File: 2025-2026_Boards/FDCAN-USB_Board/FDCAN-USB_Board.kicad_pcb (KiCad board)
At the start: 2 copper layers, 54 parts, among them J1 USB4110GFA, J2 Conn_01x03_Socket, J3 Conn_01x03_Socket, J4 Conn_01x02_Pin, J5 Conn_01x02_Pin, J6 Conn_ARM_JTAG_SWD_10, U1 AMS1117-3.3, U2 USBLC6-2SC6, U3 STM32G474CETx, U4 TCAN1057AEV-Q1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

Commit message: microcontroller pin update
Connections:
- net USB_N renamed USB_DM
- net USB_P renamed USB_DP
- U3 pad 10: LED_Debug2 -> LED_RX_1
- U3 pad 12: unconnected-(U3-PA4-Pad12) -> LED_TX_1
- U3 pad 13: LED_RX_1 -> unconnected-(U3-PA5-Pad13)
- U3 pad 14: LED_TX_1 -> LED_RX_2
- U3 pad 17: LED_RX_2 -> unconnected-(U3-PB1-Pad17)
- U3 pad 2: unconnected-(U3-PC13-Pad2) -> LED_Debug1
- U3 pad 4: unconnected-(U3-PC15-Pad4) -> LED_Debug2
- U3 pad 9: LED_Debug1 -> unconnected-(U3-PA1-Pad9)
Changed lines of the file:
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@@
 	(net 37 "SWCLK")
 	(net 38 "SWDIO")
-	(net 39 "USB_N")
-	(net 40 "USB_P")
-	(net 41 "unconnected-(U3-PC15-Pad4)")
+	(net 39 "USB_DM")
+	(net 40 "USB_DP")
+	(net 41 "unconnected-(U3-PA1-Pad9)")
 	(net 42 "unconnected-(U3-PB15-Pad29)")
 	(net 43 "unconnected-(U3-PA7-Pad15)")
@@
 	(net 48 "unconnected-(U3-PF0-Pad5)")
 	(net 49 "unconnected-(U3-PA3-Pad11)")
-	(net 50 "unconnected-(U3-PC13-Pad2)")
+	(net 50 "unconnected-(U3-PB1-Pad17)")
 	(net 51 "unconnected-(U3-PB7-Pad44)")
 	(net 52 "unconnected-(U3-PA10-Pad32)")
@@
 	(net 62 "unconnected-(U3-PF1-Pad6)")
 	(net 63 "unconnected-(U3-PB5-Pad42)")
-	(net 64 "unconnected-(U3-PA4-Pad12)")
+	(net 64 "unconnected-(U3-PA5-Pad13)")
 	(net 65 "unconnected-(U3-PB10-Pad22)")
 	(footprint "Connector_PinHeader_2.54mm:PinHeader_1x02_P2.54mm_Vertical"
@@
 			(layers "F.Cu" "F.Mask" "F.Paste")
 			(roundrect_rratio 0.25)
-			(net 50 "unconnected-(U3-PC13-Pad2)")
+			(net 16 "LED_Debug1")
 			(pinfunction "PC13")
-			(pintype "bidirectional+no_connect")
+			(pintype "bidirectional")
 		)
 		(pad "3" smd roundrect
@@
 			(layers "F.Cu" "F.Mask" "F.Paste")
 			(roundrect_rratio 0.25)
-			(net 41 "unconnected-(U3-PC15-Pad4)")
+			(net 18 "LED_Debug2")
 			(pinfunction "PC15")
-			(pintype "bidirectional+no_connect")
+			(pintype "bidirectional")
 		)
 		(pad "5" smd roundrect
@@
 			(layers "F.Cu" "F.Mask" "F.Paste")
 			(roundrect_rratio 0.25)
-			(net 16 "LED_Debug1")
+			(net 41 "unconnected-(U3-PA1-Pad9)")
 			(pinfunction "PA1")
-			(pintype "bidirectional")
+			(pintype "bidirectional+no_connect")
 		)
 		(pad "10" smd roundrect
@@
 			(layers "F.Cu" "F.Mask" "F.Paste")
 			(roundrect_rratio 0.25)
-			(net 18 "LED_Debug2")
+			(net 9 "LED_RX_1")
 			(pinfunction "PA2")
 			(pintype "bidirectional")
@@
 			(layers "F.Cu" "F.Mask" "F.Paste")
 			(roundrect_rratio 0.25)
-			(net 64 "unconnected-(U3-PA4-Pad12)")
+			(net 7 "LED_TX_1")
 			(pinfunction "PA4")
-			(pintype "bidirectional+no_connect")
+			(pintype "bidirectional")
 		)
 		(pad "13" smd roundrect
@@
 			(layers "F.Cu" "F.Mask" "F.Paste")
 			(roundrect_rratio 0.25)
-			(net 9 "LED_RX_1")
+			(net 64 "unconnected-(U3-PA5-Pad13)")
 			(pinfunction "PA5")
-			(pintype "bidirectional")
+			(pintype "bidirectional+no_connect")
 		)
 		(pad "14" smd roundrect
@@
 			(layers "F.Cu" "F.Mask" "F.Paste")
 			(roundrect_rratio 0.25)
-			(net 7 "LED_TX_1")
+			(net 13 "LED_RX_2")
 			(pinfunction "PA6")
 			(pintype "bidirectional")
@@
 			(layers "F.Cu" "F.Mask" "F.Paste")
 			(roundrect_rratio 0.25)
-			(net 13 "LED_RX_2")
+			(net 50 "unconnected-(U3-PB1-Pad17)")
 			(pinfunction "PB1")
-			(pintype "bidirectional")
+			(pintype "bidirectional+no_connect")
 		)
 		(pad "18" smd roundrect
@@
 			(layers "F.Cu" "F.Mask" "F.Paste")
 			(roundrect_rratio 0.25)
-			(net 39 "USB_N")
+			(net 39 "USB_DM")
 			(pinfunction "PA11")
 			(pintype "bidirectional")
@@
 			(layers "F.Cu" "F.Mask" "F.Paste")
 			(roundrect_rratio 0.25)
-			(net 40 "USB_P")
+			(net 40 "USB_DP")
 			(pinfunction "PA12")
 			(pintype "bidirectional")
@@
 			(layers "F.Cu" "F.Mask" "F.Paste")
 			(roundrect_rratio 0.125)
-			(net 39 "USB_N")
+			(net 39 "USB_DM")
 			(pintype "bidirectional")
 			(solder_mask_margin 0.102)
@@
 			(layers "F.Cu" "F.Mask" "F.Paste")
 			(roundrect_rratio 0.125)
-			(net 40 "USB_P")
+			(net 40 "USB_DP")
 			(pintype "bidirectional")
 			(solder_mask_margin 0.102)

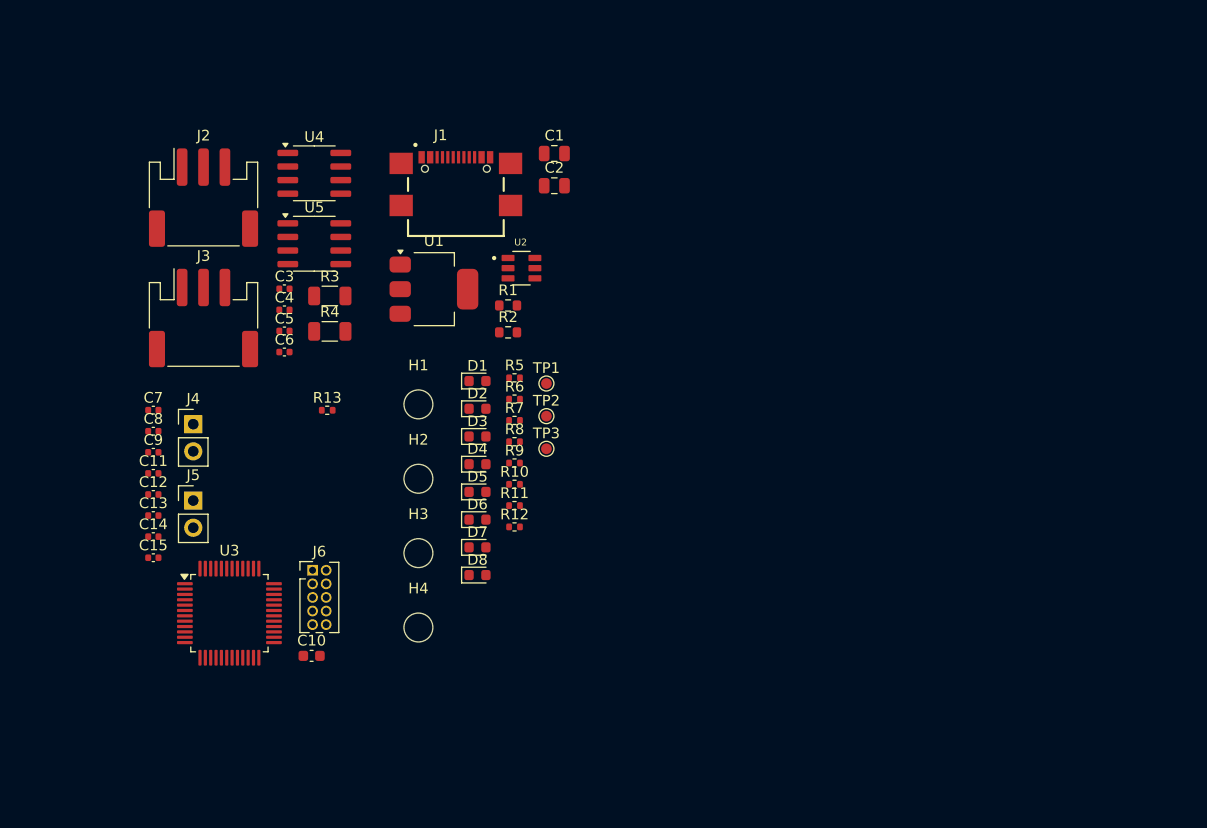
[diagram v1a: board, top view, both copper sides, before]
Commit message: grouped components
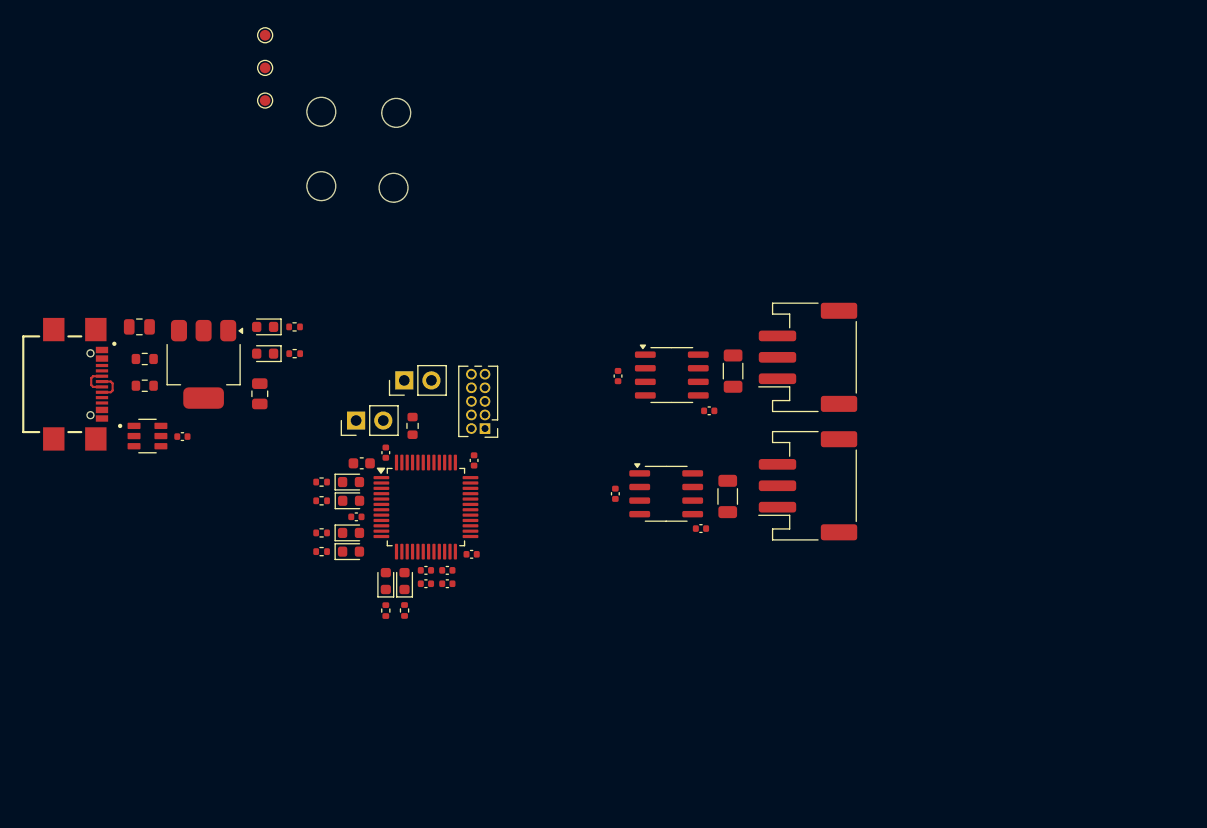
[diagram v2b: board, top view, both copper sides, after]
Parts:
- added C16: 100n, Capacitor_SMD:C_0402_1005Metric, F.Cu at (90.0, 86.2)
- R13: footprint Resistor_SMD:R_0402_1005Metric -> Resistor_SMD:R_0603_1608Metric
- moved J3 58.6 mm to (148.5, 90.8), turned to 90 degrees
- moved J2 58.4 mm to (148.5, 78.8), turned to 90 degrees
- moved C6 42.3 mm to (138.5, 94.8)
- moved H3 42.2 mm to (103.0, 55.9)
- moved H4 42.2 mm to (103.0, 62.9)
- moved C1 42.0 mm to (86.0, 76.0), turned to 180 degrees
- moved TP1 41.8 mm to (97.8, 48.8)
- moved TP2 41.8 mm to (97.8, 51.8)
- moved TP3 41.8 mm to (97.8, 54.9)
- moved C4 40.8 mm to (139.2, 83.8)
- moved U5 40.3 mm to (135.2, 91.6)
- moved R4 40.3 mm to (141.0, 91.8), turned to 90 degrees
- moved J1 39.6 mm to (81.4, 81.4), turned to -90 degrees
- moved U4 38.4 mm to (135.8, 80.5)
- moved R3 38.3 mm to (141.5, 80.1), turned to 90 degrees
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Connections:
- U2 pad 1: USB_DM -> USB+
- U2 pad 3: USB_DP -> USB-
- U2 pad 4: USB+ -> USB_DM
- U2 pad 6: USB- -> USB_DP
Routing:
- net USB-: track 0.00 -> 2.80 mm
- net USB+: track 0.00 -> 2.79 mm

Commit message: Layout work
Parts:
- moved H4 84.8 mm to (179.2, 100.0), turned to 90 degrees
- moved R9 81.4 mm to (170.8, 51.8), turned to 0 degrees
- moved R12 81.0 mm to (170.8, 50.0), turned to 0 degrees
- moved R11 80.9 mm to (170.8, 48.2), turned to 0 degrees
- moved R10 79.5 mm to (170.8, 53.6), turned to 0 degrees
- moved D6 77.2 mm to (168.0, 50.0), turned to 180 degrees
- moved D5 77.0 mm to (168.0, 48.2), turned to 180 degrees
- moved D3 76.9 mm to (168.0, 51.8), turned to 180 degrees
- moved R8 76.5 mm to (170.8, 56.6), turned to 0 degrees
- moved R7 75.0 mm to (170.8, 58.3), turned to 0 degrees
- moved D4 74.9 mm to (168.0, 53.6), turned to 180 degrees
- moved D8 71.7 mm to (168.0, 56.6), turned to 180 degrees
- moved H1 70.5 mm to (179.2, 75.0), turned to 90 degrees
- moved D7 70.0 mm to (168.0, 58.3), turned to 180 degrees
- moved J5 69.4 mm to (174.0, 52.5), turned to 0 degrees
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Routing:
- net USB-: track 2.80 -> 0.00 mm
- net USB+: track 2.79 -> 0.00 mm
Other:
- board outline added: 63.2 x 34 mm

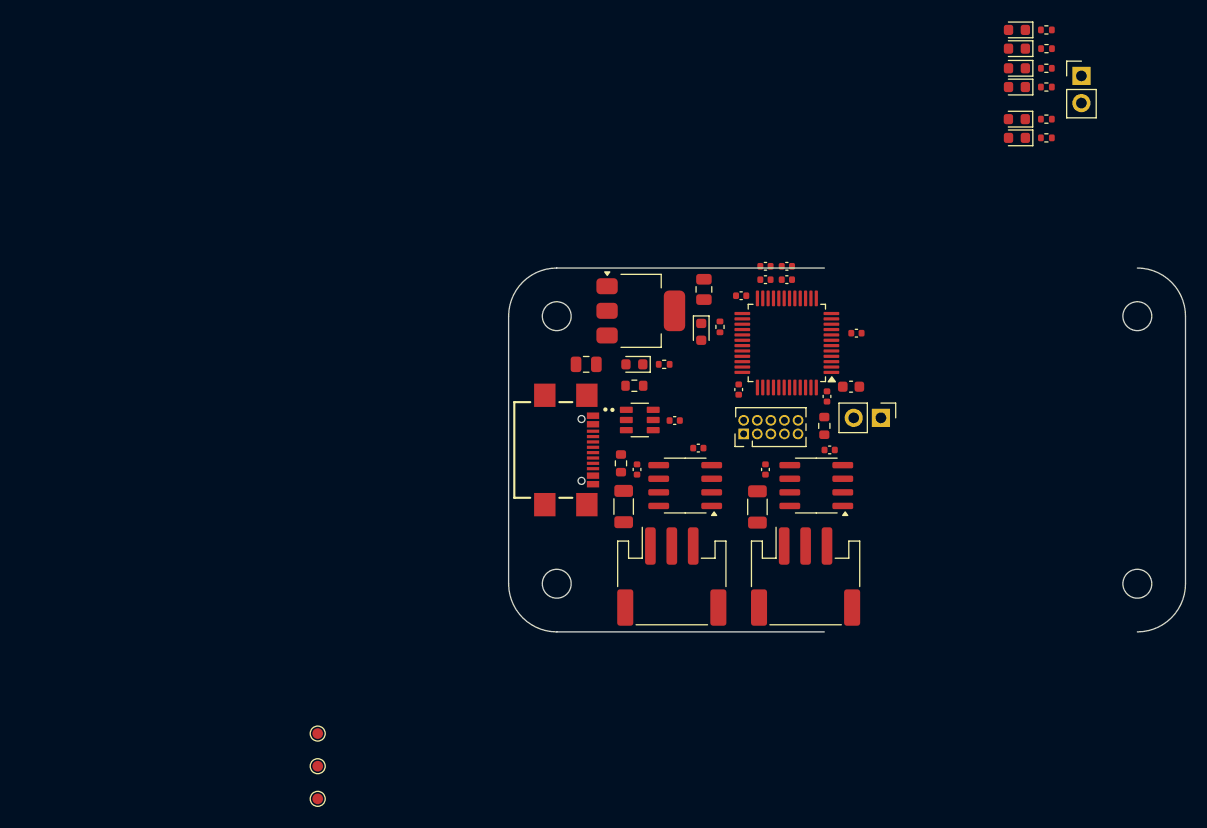
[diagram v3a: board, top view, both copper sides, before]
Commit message: Finished arranging components
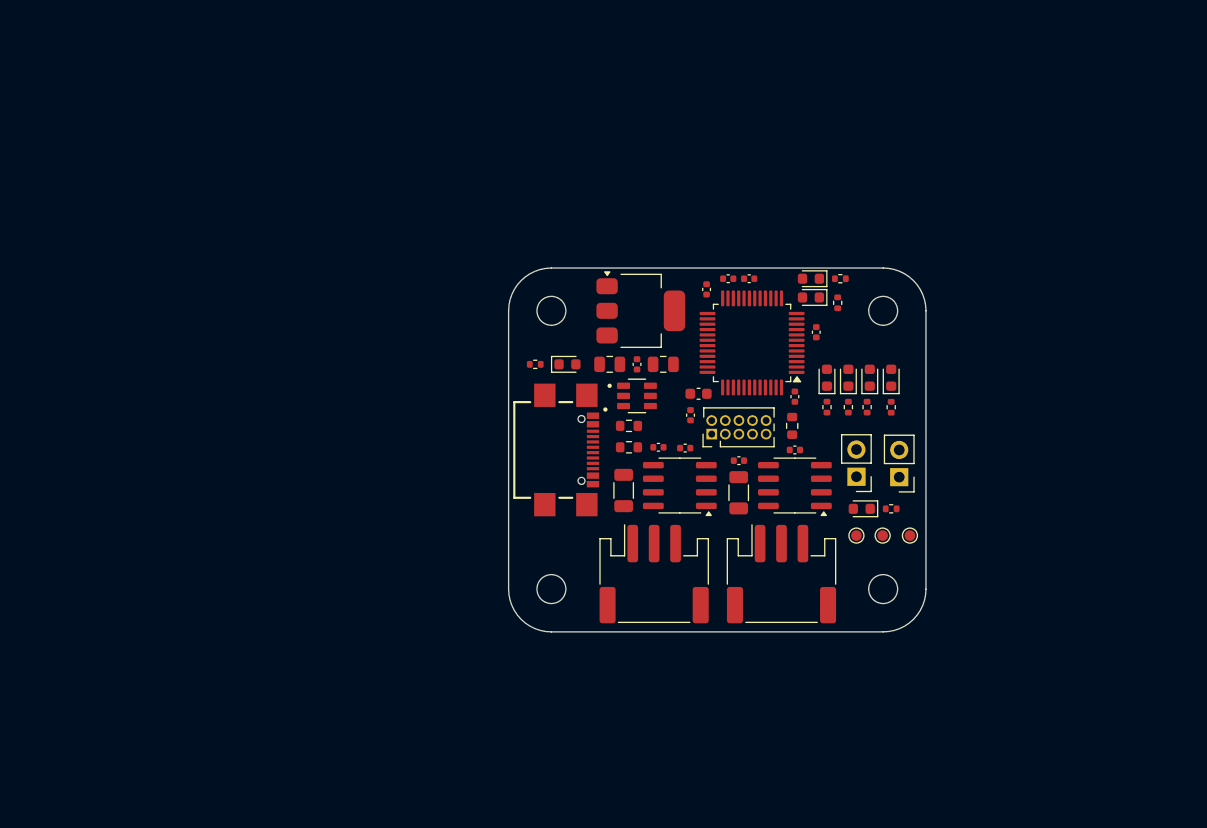
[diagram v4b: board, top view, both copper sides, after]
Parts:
- removed C13: 100n, Capacitor_SMD:C_0402_1005Metric
- removed C14: 1u, Capacitor_SMD:C_0402_1005Metric
- moved TP1 58.3 mm to (158.0, 95.5), turned to -90 degrees
- moved TP2 57.0 mm to (155.4, 95.5), turned to -90 degrees
- moved TP3 56.0 mm to (153.0, 95.5), turned to -90 degrees
- moved J5 41.2 mm to (157.0, 90.0), turned to 180 degrees
- moved R9 36.7 mm to (152.2, 83.5), turned to -90 degrees
- moved R10 36.3 mm to (150.2, 83.5), turned to -90 degrees
- moved D3 32.9 mm to (152.2, 80.8), turned to 90 degrees
- moved D4 32.4 mm to (150.2, 80.8), turned to 90 degrees
- moved R12 30.7 mm to (151.2, 73.8), turned to -90 degrees
- moved R8 30.6 mm to (156.2, 83.5), turned to -90 degrees
- moved R7 30.2 mm to (154.0, 83.5), turned to -90 degrees
- moved D5 30.2 mm to (148.8, 71.5)
- moved D6 30.2 mm to (148.8, 73.2)
- moved R11 30.2 mm to (151.5, 71.5)
- moved D8 26.9 mm to (156.2, 80.8), turned to 90 degrees
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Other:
- board size 63.2 x 34 mm -> 39 x 34 mm

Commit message: Layout finished
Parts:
- removed J1: USB4110GFA, Cornell_Mars_Rover:GCT_USB4110GFA
- added C13: 1u, Capacitor_SMD:C_0402_1005Metric, F.Cu at (92.5, 70.5)
- added C14: 1u, Capacitor_SMD:C_0402_1005Metric, F.Cu at (96.3, 68.0)
- added D5: GREEN, LED_SMD:LED_0603_1608Metric, F.Cu at (103.0, 52.5)
- added D8: YELLOW, LED_SMD:LED_0603_1608Metric, F.Cu at (103.0, 55.5)
- added G***: LOGO, Cornell_Mars_Rover:CMR_Logo, F.Cu at (119.0, 61.8)
- added J7: USB4110-GF-A, Cornell_Mars_Rover:USB4110-GF-A_GCT, F.Cu at (79.5, 64.0)
- added R14: 1k, Resistor_SMD:R_0402_1005Metric, F.Cu at (103.3, 51.0)
- added R15: 1k, Resistor_SMD:R_0402_1005Metric, F.Cu at (103.3, 54.0)
- added U6: TCAN1057AEV-Q1, Package_SO:SOIC-8_3.9x4.9mm_P1.27mm, F.Cu at (88.0, 71.2)
- D10: renamed from D8; value YELLOW -> BLUE
- D6: renamed from D4; value GREEN -> YELLOW
- D7: renamed from D6; value GREEN -> YELLOW
- D9: renamed from D7; value YELLOW -> BLUE
- J4: value Conn_01x02_Pin -> Conn_01x03_Socket; footprint Connector_PinHeader_2.54mm:PinHeader_1x02_P2.54mm_Vertical -> Connector_JST:JST_PH_S3B-PH-SM4-TB_1x03-1MP_P2.00mm_Horizontal
- R13: value 10k -> 120; footprint Resistor_SMD:R_0603_1608Metric -> Resistor_SMD:R_1206_3216Metric
- moved R6 79.8 mm to (87.5, 52.5), turned to 90 degrees
- moved TP2 78.9 mm to (90.0, 51.5)
- moved TP1 75.8 mm to (96.2, 51.5), turned to 180 degrees
- moved TP3 75.7 mm to (80.0, 75.5)
- moved D2 74.9 mm to (89.8, 53.8), turned to 0 degrees
- moved R8 74.4 mm to (87.5, 55.0), turned to 90 degrees
- moved R7 71.4 mm to (87.5, 57.5), turned to 90 degrees
- moved D10 71.1 mm to (89.7, 55.8), turned to 0 degrees
- moved D9 68.5 mm to (89.7, 57.8), turned to 0 degrees
- moved J4 65.6 mm to (88.2, 79.5), turned to 0 degrees
- moved R13 65.4 mm to (82.8, 73.2), turned to 90 degrees
- moved C4 57.9 mm to (88.0, 67.8), turned to 0 degrees
- moved J5 53.0 mm to (111.2, 63.2)
- moved R9 51.7 mm to (112.0, 51.0), turned to 180 degrees
- moved R2 51.4 mm to (85.8, 62.3), turned to -90 degrees
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- renumbered D5 to D4
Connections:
- net CANH1 renamed CAN1+
- net CANH2 renamed CAN2+
- net CANL1 renamed CAN1-
- net CANL2 renamed CAN2-
- net USB_DM renamed USB_N
- net USB_DP renamed USB_P
- J4 pad 1: 3.3V -> CAN3+
- J4 pad 2: BOOT0 -> CAN3-
- R1 pad 1: Net-(J1-CC2) -> GND
- R1 pad 2: GND -> Net-(J7-CC2)
- R13 pad 1: BOOT0 -> CAN3+
- R13 pad 2: GND -> CAN3-
- R2 pad 1: Net-(J1-CC1) -> GND
- R2 pad 2: GND -> Net-(J7-CC1)
- U3 pad 10: LED_RX_1 -> LED_TX_1
- U3 pad 12: LED_TX_1 -> LED_RX_2
- U3 pad 13: unconnected-(U3-PA5-Pad13) -> LED_TX_2
- U3 pad 14: LED_RX_2 -> unconnected-(U3-PA6-Pad14)
- U3 pad 16: LED_TX_2 -> LED_RX_3
- U3 pad 17: unconnected-(U3-PB1-Pad17) -> LED_TX_3
- U3 pad 2: LED_Debug1 -> unconnected-(U3-PC13-Pad2)
- U3 pad 25: unconnected-(U3-PB11-Pad25) -> LED_Debug2
- U3 pad 26: CAN_RX1 -> LED_Debug1
- U3 pad 27: CAN_TX1 -> unconnected-(U3-PB13-Pad27)
- U3 pad 30: CAN_RX2 -> CAN_RX3
- U3 pad 39: CAN_TX2 -> CAN_TX3
- U3 pad 4: LED_Debug2 -> unconnected-(U3-PC15-Pad4)
- U3 pad 42: unconnected-(U3-PB5-Pad42) -> CAN_RX2
- U3 pad 43: unconnected-(U3-PB6-Pad43) -> CAN_TX2
- U3 pad 45: BOOT0 -> CAN_RX1
- U3 pad 46: unconnected-(U3-PB9-Pad46) -> CAN_TX1
- U3 pad 9: unconnected-(U3-PA1-Pad9) -> LED_RX_1
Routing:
- net 3.3V: track 0.00 -> 103.4 mm, vias 0 -> 3
- net 5V: track 0.00 -> 83.4 mm, vias 0 -> 7
- net GND: track 0.00 -> 56.8 mm, vias 0 -> 48
- net CAN_TX1: track 0.00 -> 22.4 mm, vias 0 -> 2
- net CAN_RX1: track 0.00 -> 19.2 mm
- net SWDIO: track 0.00 -> 13.9 mm, vias 0 -> 1
- net LED_TX_1: track 0.00 -> 13.7 mm
- net SWCLK: track 0.00 -> 13.2 mm, vias 0 -> 1
- net CAN_TX2: track 0.00 -> 12.8 mm, vias 0 -> 2
- net USB+: track 0.00 -> 12.6 mm, vias 0 -> 2
- net SWO: track 0.00 -> 12.3 mm, vias 0 -> 1
- net USB-: track 0.00 -> 12.2 mm, vias 0 -> 2
- net NRST: track 0.00 -> 11.8 mm
- net LED_RX_1: track 0.00 -> 11.5 mm
- net CAN_TX3: track 0.00 -> 11.2 mm
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- added copper zone on B.Cu, net GND
- added copper zone on F.Cu, net GND
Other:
- board size 39 x 34 mm -> 50.5 x 34.8 mm
- board text added: "1"
- board text added: "2"
- board text added: "3"
- board text added: "3V3"
- board text added: "5V"
- board text added: "DB1"
- board text added: "DB2"
- board text added: "Dawson Melton"
- board text added: "GND"
- board text added: "RX"
- board text added: "TX"

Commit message: Gerber files, BOM, layout fix
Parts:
- moved U1 0.25 mm to (121.5, 70.8)
